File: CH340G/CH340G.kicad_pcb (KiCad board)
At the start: 2 copper layers, 15.2 x 25.4 mm, 25 parts, among them J2 Conn_01x06, P1 USB_C_Plug_USB2.0, U1 CH340G, U2 AP2127K-3.3, Y1 Crystal_GND24

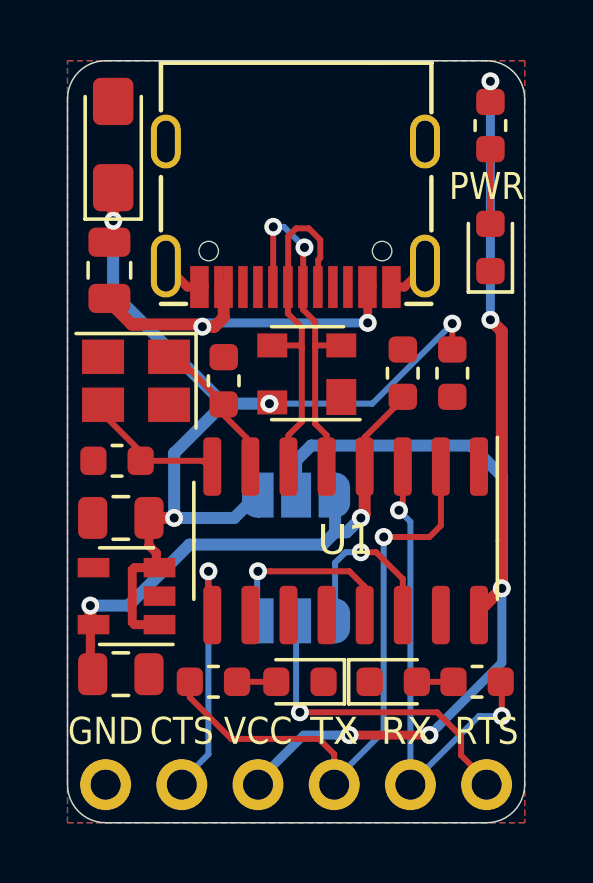
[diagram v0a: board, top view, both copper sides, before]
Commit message: SirUSB Updates
3D Renders changed to white solder mask. CH330N TX and RX references moved
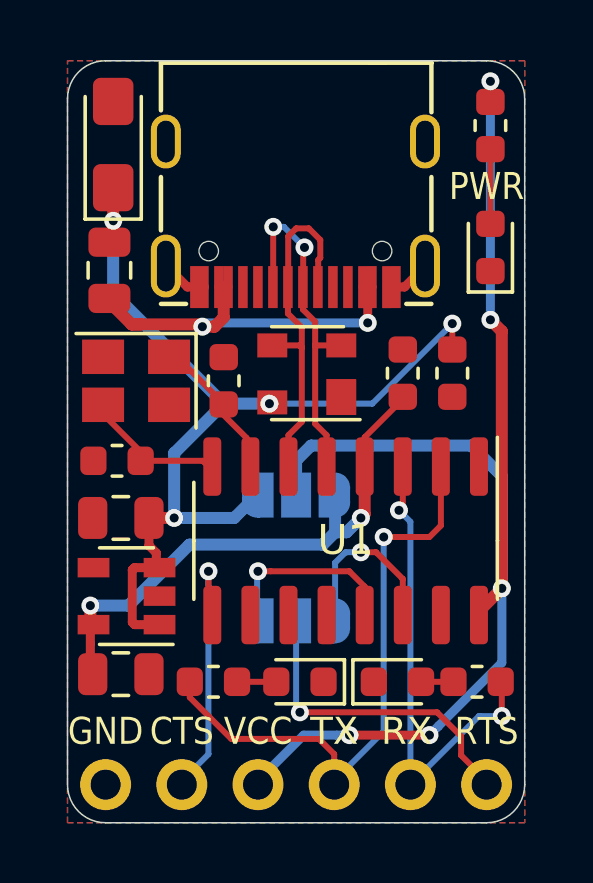
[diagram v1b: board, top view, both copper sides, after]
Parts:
- moved RX1 0.14 mm to (73.7, 48.4)
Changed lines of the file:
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@@
   )
   (module LED_SMD:LED_0603_1608Metric (layer F.Cu)
-    (at 73.5965 48.387)
+    (at 73.7362 48.387)
     (descr "LED SMD 0603 (1608 Metric), square (rectangular) end terminal, IPC_7351 nominal, (Body size source: http://www.tortai-tech.com/upload/download/2011102023233369053.pdf), generated with kicad-footprint-generator")
     (tags diode)

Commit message: CH340G Fix
5k1 Resistors added to CC1 and CC2, TX and RX LEDs pulled up to VCC,Copper Pour changed from 3V3 to VCC.
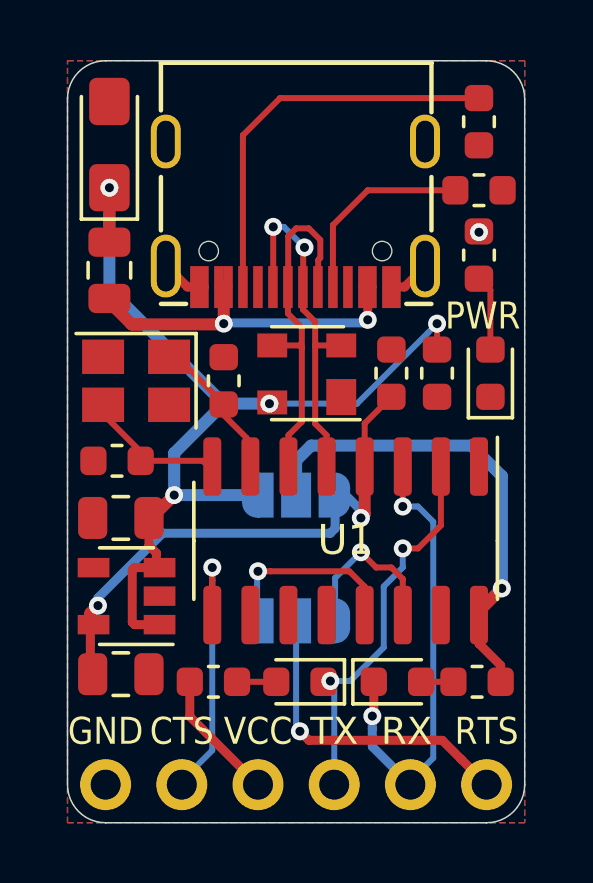
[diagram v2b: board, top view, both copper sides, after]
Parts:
- added R4: 5K1, Resistor_SMD:R_0603_1608Metric, F.Cu at (76.5, 29.7)
- added R5: 5K1, Resistor_SMD:R_0603_1608Metric, F.Cu at (76.5, 32.0)
- Pin6: renamed from Pin 6
- moved R1 4.33 mm to (76.5, 34.2)
- moved PWR 4.19 mm to (76.8, 38.1)
- moved C4 0.51 mm to (75.1, 38.1)
- moved C5 0.38 mm to (73.5, 38.1)
- moved C3 0.13 mm to (64.1, 30.5)
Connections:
- R2 pad 1: TX -> VCC
- R3 pad 1: RX -> VCC
- RX1 pad 1: GND -> RX
- TX2 pad 1: GND -> TX
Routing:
- net VCC: track 43.6 -> 20.7 mm, vias 5 -> 2
- net Net-(P1-PadB5): track 0.00 -> 13.4 mm
- net TX: track 19.9 -> 12.7 mm, vias 1 -> 2
- net Net-(P1-PadA5): track 0.00 -> 6.63 mm
- net Net-(F1-Pad2): track 13.4 -> 12.8 mm
- added copper zone on B.Cu, net VCC
- removed copper zone on B.Cu, net 3V3
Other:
- board text added: "USB"

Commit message: SiRUSB Updates
USB-C 3D Renders Added and Pictures Updated
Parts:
- J2: footprint Connector_PinHeader_2.54mm:PinHeader_1x06_P2.54mm_Vertical -> Connector_PinHeader_2.54mm:PinHeader_1x06_P2.54mm_Horizontal; moved to F.Cu
- turned J2 to 270 degrees

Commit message: SirUSB Board Revisions
Removed MicroUSB Versions of FT230 and FT231, SolderPaste Layer Adjusted to -0.05mm, Silkscreens optimised, OSHW logo added.
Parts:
- added G***: LOGO, logo:OSHW36x26, B.Cu at (76.5, 32.4)
- G***: footprint logo:SirBoard98x31 -> logo:SirBoard112x35
- moved G*** 0.15 mm to (70.4, 37.8)
